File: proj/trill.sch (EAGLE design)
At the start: 122 parts, among them J1 SPKRAST_01532MR, J2 MICCMA-4544PF-W, J3 ADAFRUIT_OLED_13, J4 DM3D-SFDM, J5 SJ1-3523N, J6 CONUFL001, M1 Z3OC_VIB_MOTOR, U1 SIM5300EA, U10 3.3V 600mA, U11 MCP1642B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

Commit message: Further routed Trill mobile phone board
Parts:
- added C56: 100uF, dooba:CAP1210
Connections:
- net 5.0V: now also C56.1
- net GND: now also C56.2
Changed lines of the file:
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@@
 <part name="BAT[+-]" library="dooba" deviceset="PIN_2" device=""/>
 <part name="GND133" library="supply1" library_urn="urn:adsk.eagle:library:371" deviceset="GND" device=""/>
+<part name="C56" library="dooba" deviceset="CAP" device="1210" value="100uF"/>
+<part name="GND137" library="supply1" library_urn="urn:adsk.eagle:library:371" deviceset="GND" device=""/>
 </parts>
 <sheets>
@@
 <instance part="BAT[+-]" gate="P1" x="33.02" y="756.92" rot="R90"/>
 <instance part="GND133" gate="1" x="35.56" y="744.22"/>
+<instance part="C56" gate="C1" x="63.5" y="728.98" rot="R180"/>
+<instance part="GND137" gate="1" x="48.26" y="728.98" rot="R270"/>
 </instances>
 <busses>
@@
 <wire x1="35.56" y1="749.3" x2="35.56" y2="746.76" width="0.1524" layer="91"/>
 </segment>
+<segment>
+<pinref part="C56" gate="C1" pin="2"/>
+<pinref part="GND137" gate="1" pin="GND"/>
+<wire x1="50.8" y1="728.98" x2="53.34" y2="728.98" width="0.1524" layer="91"/>
+</segment>
 </net>
 <net name="N$28" class="0">
@@
 <pinref part="C26" gate="C1" pin="2"/>
 <wire x1="73.66" y1="721.36" x2="76.2" y2="721.36" width="0.1524" layer="91"/>
-<wire x1="73.66" y1="721.36" x2="73.66" y2="736.6" width="0.1524" layer="91"/>
+<wire x1="73.66" y1="721.36" x2="73.66" y2="728.98" width="0.1524" layer="91"/>
 <junction x="73.66" y="721.36"/>
 <label x="-15.24" y="736.6" size="1.778" layer="95"/>
+<wire x1="73.66" y1="728.98" x2="73.66" y2="736.6" width="0.1524" layer="91"/>
 <wire x1="73.66" y1="736.6" x2="-17.78" y2="736.6" width="0.1524" layer="91"/>
-</segment>
-<segment>
+<pinref part="C56" gate="C1" pin="1"/>
+<junction x="73.66" y="728.98"/>
+</segment>
+<segment>

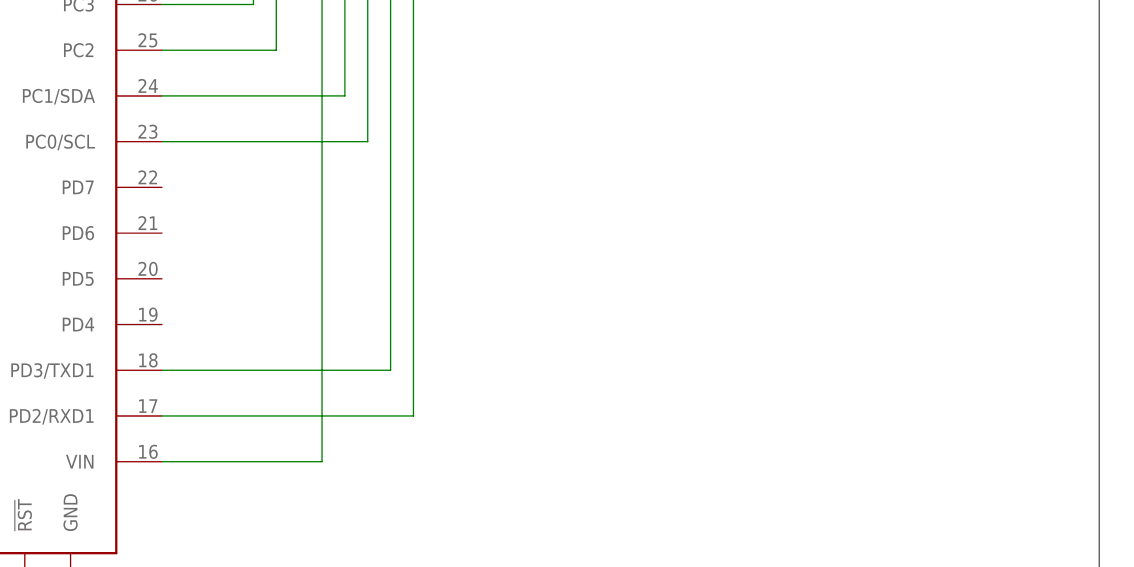
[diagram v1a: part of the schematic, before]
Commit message: Added 2 LEDs (PWM-able) to Trill Mobile Phone
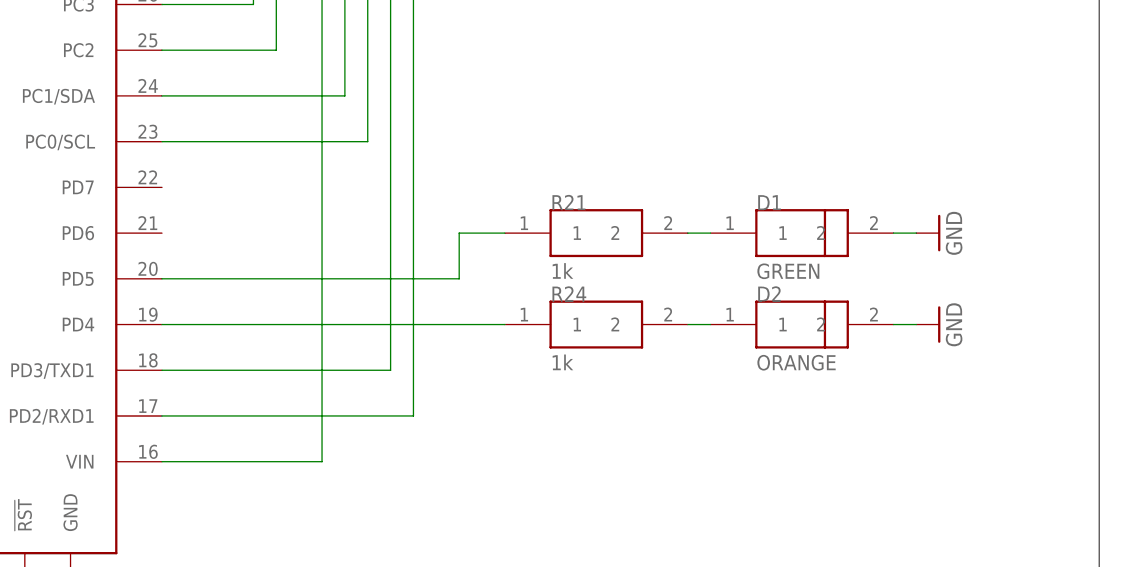
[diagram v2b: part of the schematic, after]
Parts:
- added D1: GREEN, dooba:LED0805
- added D2: ORANGE, dooba:LED0805
- added R21, R24: 1k, dooba:RES0805
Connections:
- new net N$63: D1.1, R21.2
- new net N$64: D2.1, R24.2
- new net N$65: N1.PD4, R24.1
- new net N$66: N1.PD5, R21.1
- net GND: now also D1.2, D2.2
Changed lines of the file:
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@@
 <part name="C56" library="dooba" deviceset="CAP" device="1210" value="100uF"/>
 <part name="GND137" library="supply1" library_urn="urn:adsk.eagle:library:371" deviceset="GND" device=""/>
+<part name="D1" library="dooba" deviceset="LED" device="0805" value="GREEN"/>
+<part name="D2" library="dooba" deviceset="LED" device="0805" value="ORANGE"/>
+<part name="R21" library="dooba" deviceset="RES" device="0805" value="1k"/>
+<part name="R24" library="dooba" deviceset="RES" device="0805" value="1k"/>
+<part name="GND138" library="supply1" library_urn="urn:adsk.eagle:library:371" deviceset="GND" device=""/>
+<part name="GND139" library="supply1" library_urn="urn:adsk.eagle:library:371" deviceset="GND" device=""/>
 </parts>
 <sheets>
@@
 <instance part="C56" gate="C1" x="63.5" y="728.98" rot="R180"/>
 <instance part="GND137" gate="1" x="48.26" y="728.98" rot="R270"/>
+<instance part="D1" gate="D1" x="414.02" y="393.7"/>
+<instance part="D2" gate="D1" x="414.02" y="383.54"/>
+<instance part="R21" gate="R1" x="391.16" y="393.7"/>
+<instance part="R24" gate="R1" x="391.16" y="383.54"/>
+<instance part="GND138" gate="1" x="429.26" y="393.7" rot="R90"/>
+<instance part="GND139" gate="1" x="429.26" y="383.54" rot="R90"/>
 </instances>
 <busses>
@@
 <wire x1="50.8" y1="728.98" x2="53.34" y2="728.98" width="0.1524" layer="91"/>
 </segment>
+<segment>
+<pinref part="D1" gate="D1" pin="2"/>
+<pinref part="GND138" gate="1" pin="GND"/>
+<wire x1="426.72" y1="393.7" x2="424.18" y2="393.7" width="0.1524" layer="91"/>
+</segment>
+<segment>
+<pinref part="D2" gate="D1" pin="2"/>
+<pinref part="GND139" gate="1" pin="GND"/>
+<wire x1="426.72" y1="383.54" x2="424.18" y2="383.54" width="0.1524" layer="91"/>
+</segment>
 </net>
 <net name="N$28" class="0">
@@
 </segment>
 </net>
+<net name="N$63" class="0">
+<segment>
+<pinref part="D1" gate="D1" pin="1"/>
+<pinref part="R21" gate="R1" pin="2"/>
+<wire x1="403.86" y1="393.7" x2="401.32" y2="393.7" width="0.1524" layer="91"/>
+</segment>
+</net>
+<net name="N$64" class="0">
+<segment>
+<pinref part="R24" gate="R1" pin="2"/>
+<pinref part="D2" gate="D1" pin="1"/>
+<wire x1="401.32" y1="383.54" x2="403.86" y2="383.54" width="0.1524" layer="91"/>
+</segment>
+</net>
+<net name="N$65" class="0">
+<segment>
+<pinref part="N1" gate="N1" pin="PD4"/>
+<pinref part="R24" gate="R1" pin="1"/>
+<wire x1="342.9" y1="383.54" x2="381" y2="383.54" width="0.1524" layer="91"/>
+</segment>
+</net>
+<net name="N$66" class="0">
+<segment>
+<pinref part="N1" gate="N1" pin="PD5"/>
+<wire x1="342.9" y1="388.62" x2="375.92" y2="388.62" width="0.1524" layer="91"/>
+<wire x1="375.92" y1="388.62" x2="375.92" y2="393.7" width="0.1524" layer="91"/>
+<pinref part="R21" gate="R1" pin="1"/>
+<wire x1="375.92" y1="393.7" x2="381" y2="393.7" width="0.1524" layer="91"/>
+</segment>
+</net>

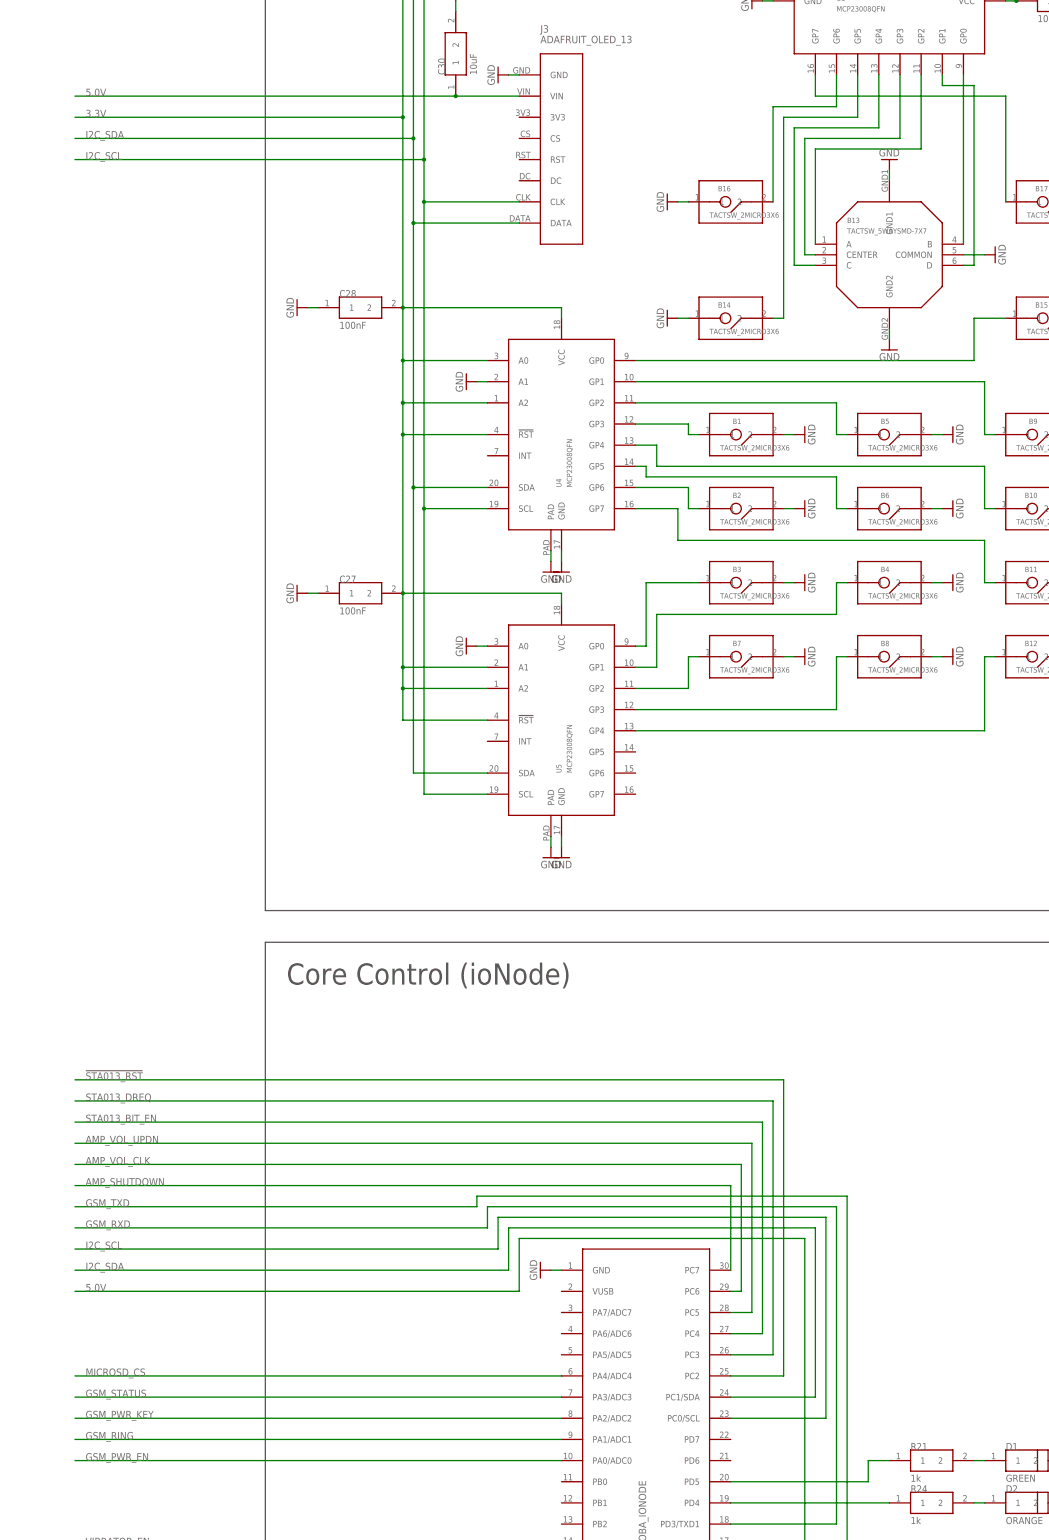
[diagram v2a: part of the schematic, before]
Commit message: Cleaned up repo Added raccoon artwork to Trill board
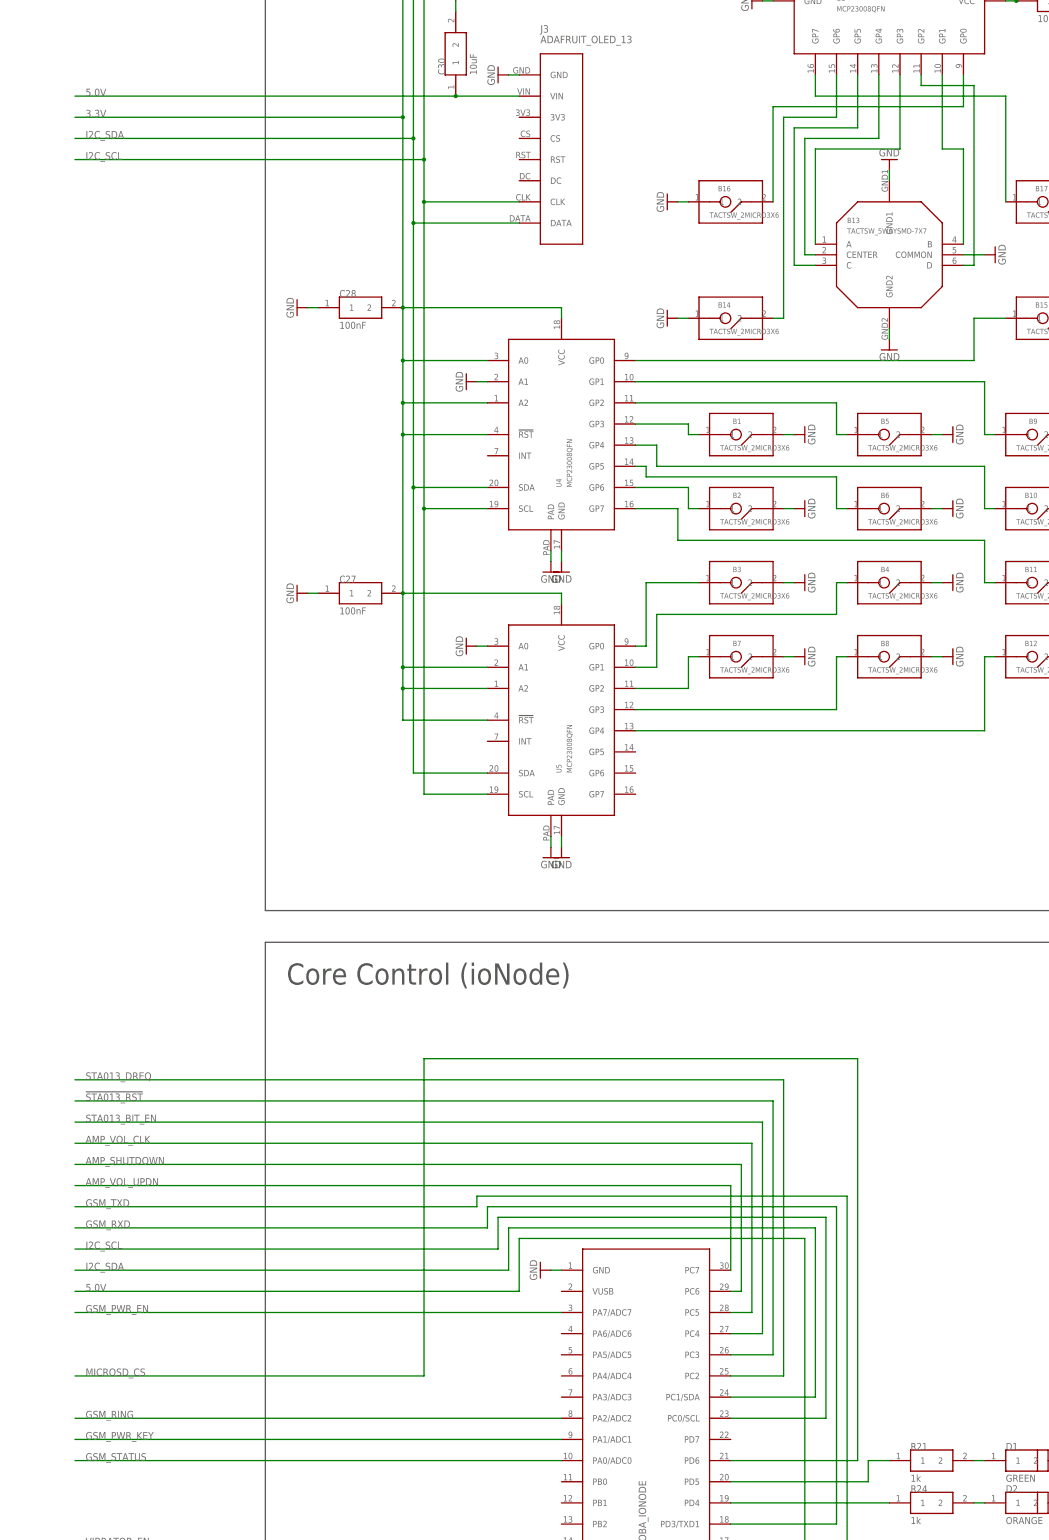
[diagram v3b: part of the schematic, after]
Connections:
- net !STA013_RST: now also N1.PC3; no longer N1.PC2
- net AMP_SHUTDOWN: now also N1.PC6; no longer N1.PC7
- net AMP_VOL_CLK: now also N1.PC5; no longer N1.PC6
- net AMP_VOL_UPDN: now also N1.PC7; no longer N1.PC5
- net GSM_PWR_EN: now also N1.PA7/ADC7; no longer N1.PA0/ADC0
- net GSM_PWR_KEY: now also N1.PA1/ADC1; no longer N1.PA2/ADC2
- net GSM_RING: now also N1.PA2/ADC2; no longer N1.PA1/ADC1
- net GSM_STATUS: now also N1.PA0/ADC0; no longer N1.PA3/ADC3
- net MICROSD_CS: now also N1.PD6; no longer N1.PA4/ADC4
- net N$1: now also U3.GP1; no longer U3.GP0
- net N$2: now also U3.GP3; no longer U3.GP2
- net N$3: now also U3.GP4; no longer U3.GP3
- net N$4: now also U3.GP5; no longer U3.GP4
- net N$5: now also U3.GP2; no longer U3.GP1
- net N$6: now also U3.GP6; no longer U3.GP5
- net N$7: now also U3.GP0; no longer U3.GP6
- net STA013_DREQ: now also N1.PC2; no longer N1.PC3

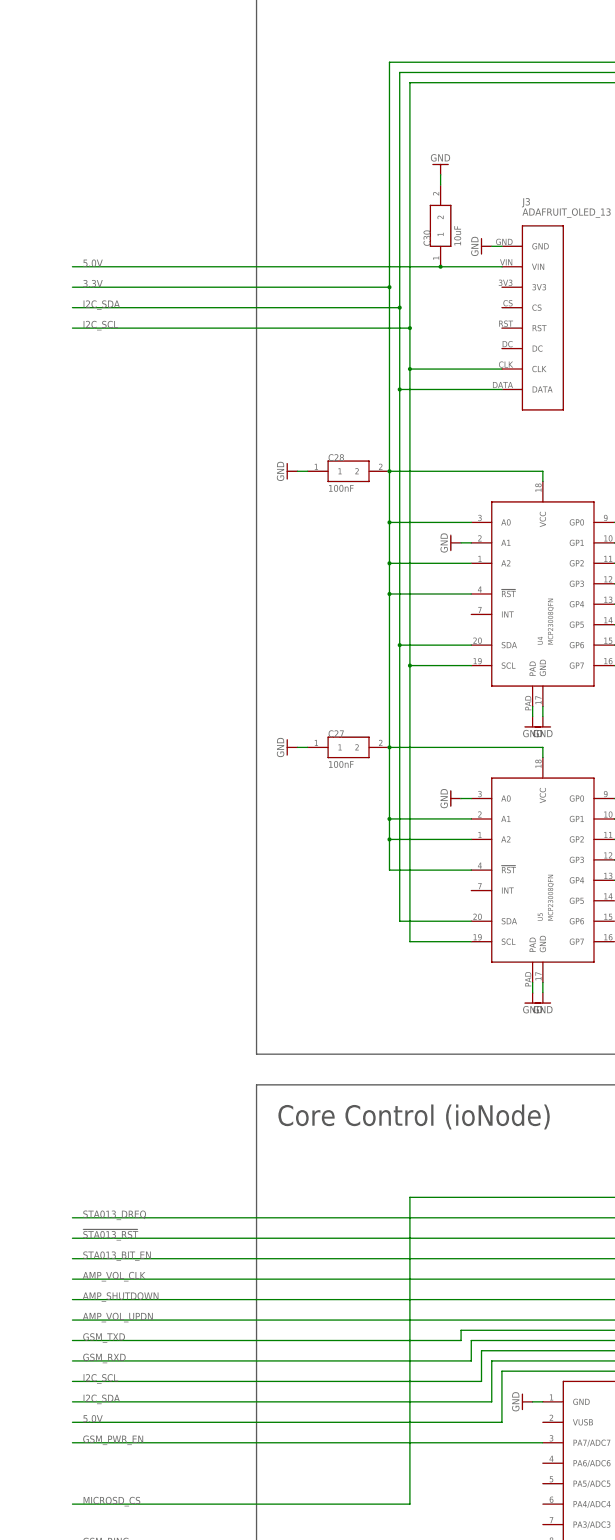
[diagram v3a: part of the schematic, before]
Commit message: Added OLED RESET line on Trill board
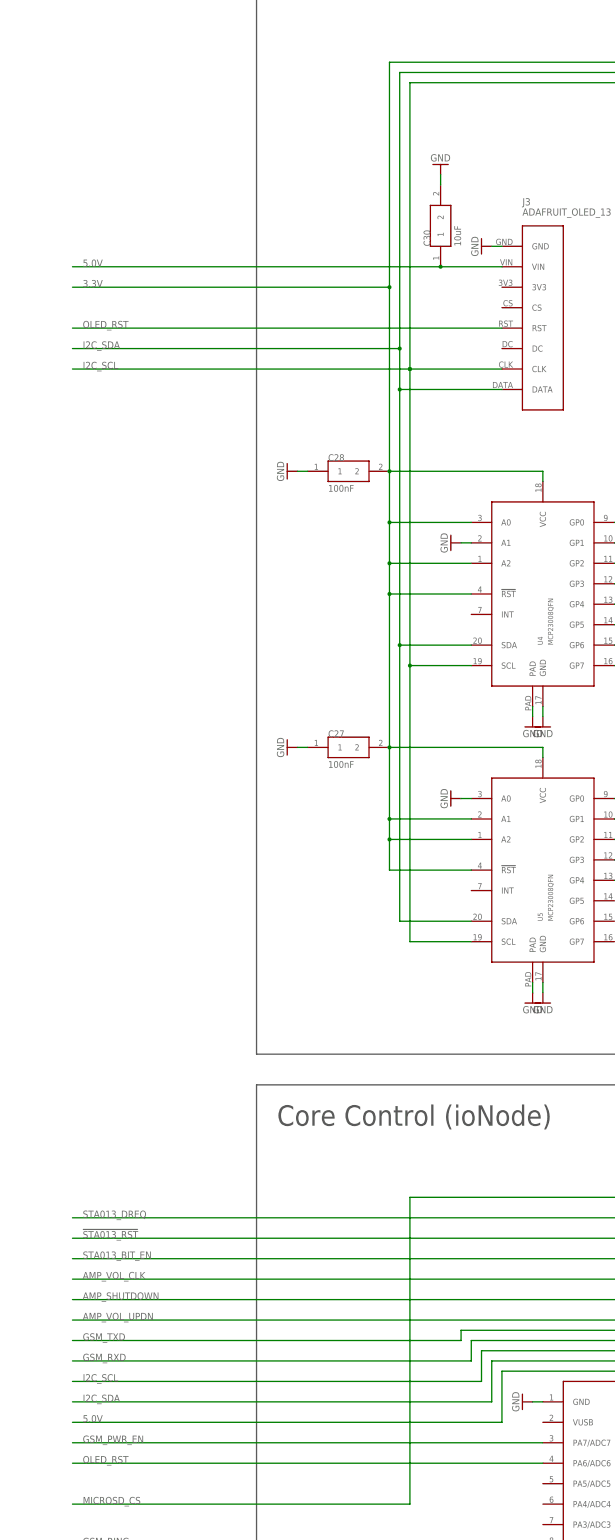
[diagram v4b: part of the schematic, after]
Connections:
- new net OLED_RST: J3.RST, N1.PA6/ADC6
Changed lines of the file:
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@@
 <?xml version="1.0" encoding="utf-8"?>
 <!DOCTYPE eagle SYSTEM "eagle.dtd">
-<eagle version="8.4.0">
+<eagle version="8.4.1">
 <drawing>
 <settings>
@@
 <wire x1="266.7" y1="627.38" x2="266.7" y2="690.88" width="0.1524" layer="91"/>
 <pinref part="U3" gate="U1" pin="SDA"/>
-<wire x1="266.7" y1="690.88" x2="266.7" y2="711.2" width="0.1524" layer="91"/>
-<wire x1="266.7" y1="711.2" x2="266.7" y2="769.62" width="0.1524" layer="91"/>
+<wire x1="266.7" y1="690.88" x2="266.7" y2="701.04" width="0.1524" layer="91"/>
+<wire x1="266.7" y1="701.04" x2="266.7" y2="769.62" width="0.1524" layer="91"/>
 <wire x1="266.7" y1="769.62" x2="368.3" y2="769.62" width="0.1524" layer="91"/>
 <wire x1="368.3" y1="769.62" x2="368.3" y2="762" width="0.1524" layer="91"/>
@@
 <wire x1="292.1" y1="690.88" x2="266.7" y2="690.88" width="0.1524" layer="91"/>
 <junction x="266.7" y="690.88"/>
-<wire x1="185.42" y1="711.2" x2="266.7" y2="711.2" width="0.1524" layer="91"/>
-<junction x="266.7" y="711.2"/>
-<label x="187.96" y="711.2" size="1.778" layer="95"/>
+<wire x1="185.42" y1="701.04" x2="266.7" y2="701.04" width="0.1524" layer="91"/>
+<junction x="266.7" y="701.04"/>
+<label x="187.96" y="701.04" size="1.778" layer="95"/>
 </segment>
 <segment>
@@
 <wire x1="269.24" y1="622.3" x2="269.24" y2="695.96" width="0.1524" layer="91"/>
 <pinref part="U3" gate="U1" pin="SCL"/>
-<wire x1="269.24" y1="695.96" x2="269.24" y2="706.12" width="0.1524" layer="91"/>
-<wire x1="269.24" y1="706.12" x2="269.24" y2="767.08" width="0.1524" layer="91"/>
+<wire x1="269.24" y1="695.96" x2="269.24" y2="767.08" width="0.1524" layer="91"/>
 <wire x1="269.24" y1="767.08" x2="363.22" y2="767.08" width="0.1524" layer="91"/>
 <wire x1="363.22" y1="767.08" x2="363.22" y2="762" width="0.1524" layer="91"/>
@@
 <wire x1="292.1" y1="695.96" x2="269.24" y2="695.96" width="0.1524" layer="91"/>
 <junction x="269.24" y="695.96"/>
-<wire x1="185.42" y1="706.12" x2="269.24" y2="706.12" width="0.1524" layer="91"/>
-<junction x="269.24" y="706.12"/>
-<label x="187.96" y="706.12" size="1.778" layer="95"/>
+<wire x1="185.42" y1="695.96" x2="269.24" y2="695.96" width="0.1524" layer="91"/>
+<junction x="269.24" y="695.96"/>
+<label x="187.96" y="695.96" size="1.778" layer="95"/>
 </segment>
 <segment>
@@
 </segment>
 </net>
+<net name="OLED_RST" class="0">
+<segment>
+<pinref part="J3" gate="J1" pin="RST"/>
+<wire x1="292.1" y1="706.12" x2="185.42" y2="706.12" width="0.1524" layer="91"/>
+<label x="187.96" y="706.12" size="1.778" layer="95"/>
+</segment>
+<segment>
+<pinref part="N1" gate="N1" pin="PA6/ADC6"/>
+<wire x1="302.26" y1="424.18" x2="185.42" y2="424.18" width="0.1524" layer="91"/>
+<label x="187.96" y="424.18" size="1.778" layer="95"/>
+</segment>
+</net>
